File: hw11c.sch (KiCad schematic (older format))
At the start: 84 parts, among them Q1 KX-7_12MHZ, SW1 BUTT1, SW2 BUTT2, X1 ~RESET, X10 PIO2.8, X11 PIO1.4, X12 ADC3, X13 PIO0.8, X14 PIO0.9, X15 MAT0, X16 PIO0.6, X17 PIO0.7, X18 ADC6, X2 SWCLK, X3 SWDIO, X4 SSEL1, X5 SCK1, X6 MISO1, X7 MOSI1, X8 PIO2.6, X9 PIO2.7

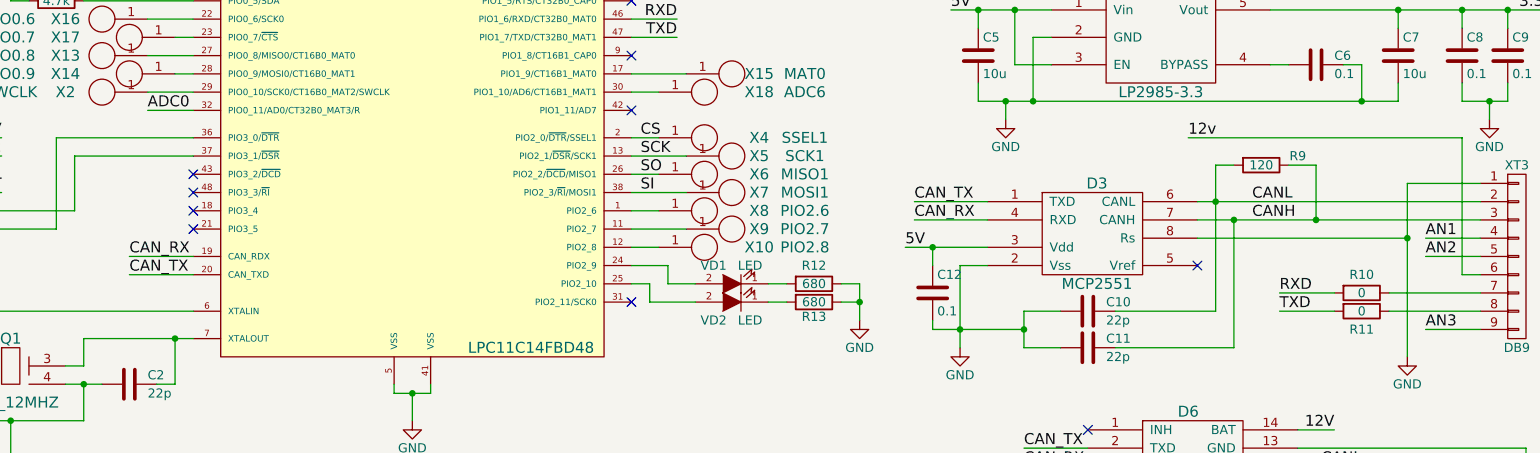
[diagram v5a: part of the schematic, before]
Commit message: Add Rs signal for MCP2551. Pin connected to MCU pin 3.4.
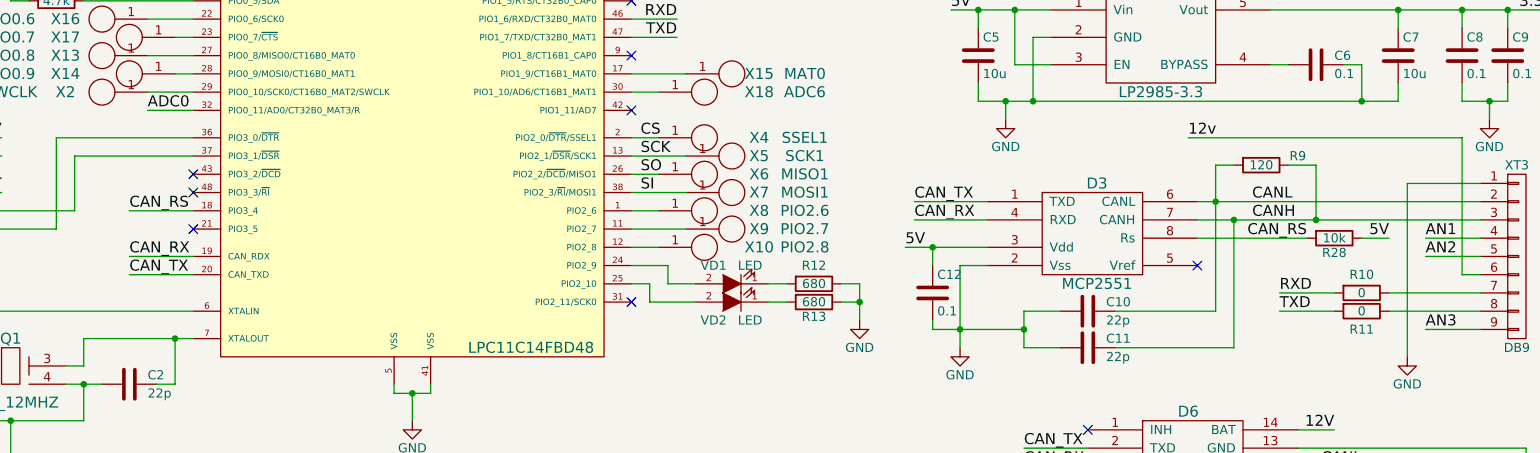
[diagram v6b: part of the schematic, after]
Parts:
- added R28: 10k, libs:R_0603, symbol R
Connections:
- net 5V: now also R28.1
- net GND: no longer D3.8 (Rs)
- net CAN_RS: now reaches D1.18 (PIO3_4)
- net CAN_RS: now also D3.8 (Rs), R28.2
- no-connect marks 13 -> 12
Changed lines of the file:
@@
 NoConn ~ 2950 3200
 NoConn ~ 2950 3300
-NoConn ~ 2950 3400
 NoConn ~ 2950 3500
 Text Label 5650 1850 2    60   ~ 0
@@
 Wire Wire Line
 	9900 3750 10000 3750
-Connection ~ 9600 3550
-Wire Wire Line
-	8450 3550 9600 3550
 Connection ~ 9100 3450
 Wire Wire Line
@@
 Wire Wire Line
 	5350 2750 5500 2750
+Text Label 9050 3550 2    60   ~ 0
+CAN_RS
+Wire Wire Line
+	8450 3550 9050 3550
+Text Label 2600 3400 0    60   ~ 0
+CAN_RS
+Wire Wire Line
+	2600 3400 2950 3400
+$Comp
+L R R28
+U 1 1 5B50A1AD
+P 9200 3550
+F 0 "R28" V 9280 3550 50  0000 C CNN
+F 1 "10k" V 9200 3550 50  0000 C CNN
+F 2 "libs:R_0603" V 9130 3550 50  0001 C CNN
+F 3 "" H 9200 3550 50  0001 C CNN
+	1    9200 3550
+	0    1    1    0
+$EndComp
+Text Label 9500 3550 2    60   ~ 0
+5V
+Wire Wire Line
+	9500 3550 9350 3550
 $EndSCHEMATC
